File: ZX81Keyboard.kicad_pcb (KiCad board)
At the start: 2 copper layers, 153 x 58 mm, 52 parts, among them J2 Conn_01x05, J3 Conn_01x03, J4 Conn_01x08, SW1 1, SW10 0, SW11 Q, SW12 W, SW13 E, SW14 R, SW15 T, SW16 Y, SW17 U, SW18 I, SW19 O, SW2 2, SW20 P, SW21 A, SW22 S, SW23 D, SW24 F, SW25 G, SW26 H, SW27 J, SW28 K, SW29 L, SW3 3, SW30 NEW_LINE, SW31 SHIFT, SW32 Z, SW33 X, SW34 C, SW35 V, SW36 B, SW37 N, SW38 M, SW39 ., SW4 4, SW40 SPACE, SW5 5, SW6 6, SW7 7, SW8 8, SW9 9

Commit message: Nearing completion.
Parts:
- added G***: LOGO, zx81keyboard:title, F.Cu at (95.5, 69.8)
- moved G*** 37.7 mm to (71.4, 69.3)
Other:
- board text added: "+"
- board text added: "GND TURBO POWER"
- board text added: "J"
- board text added: "KA15 KA14 KA8 KA13 KA9 KA12 KA10 KA11"
- board text added: "KD0 KD1 KD2 KD3 KD4"
- board text removed: "ZX81 Tactile Keyboard"

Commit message: Nearing completion.
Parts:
- moved H1 0.71 mm to (65.5, 120.5)
- moved H2 0.71 mm to (212.0, 120.5)
- moved H3 0.71 mm to (65.5, 69.0)
- moved H4 0.71 mm to (212.0, 69.0)

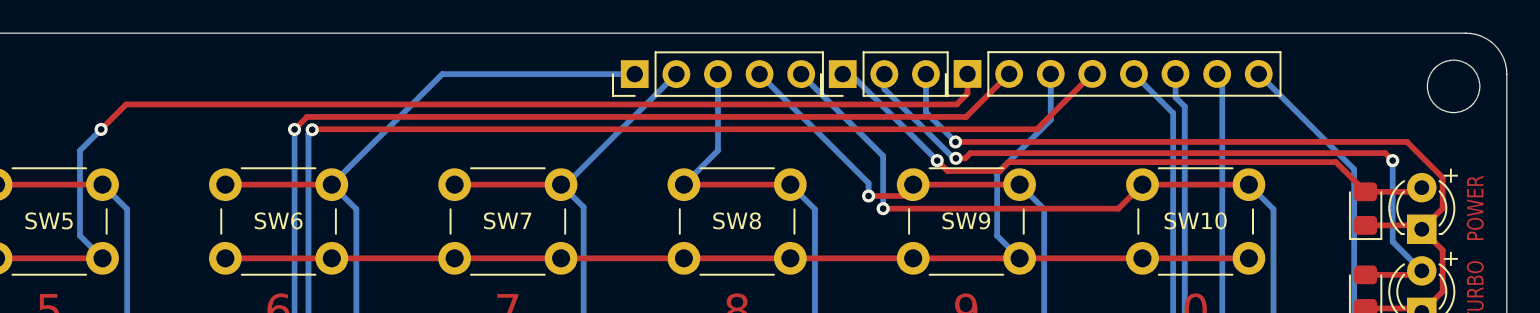
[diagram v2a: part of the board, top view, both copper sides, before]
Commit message: Fixed connector orientation.
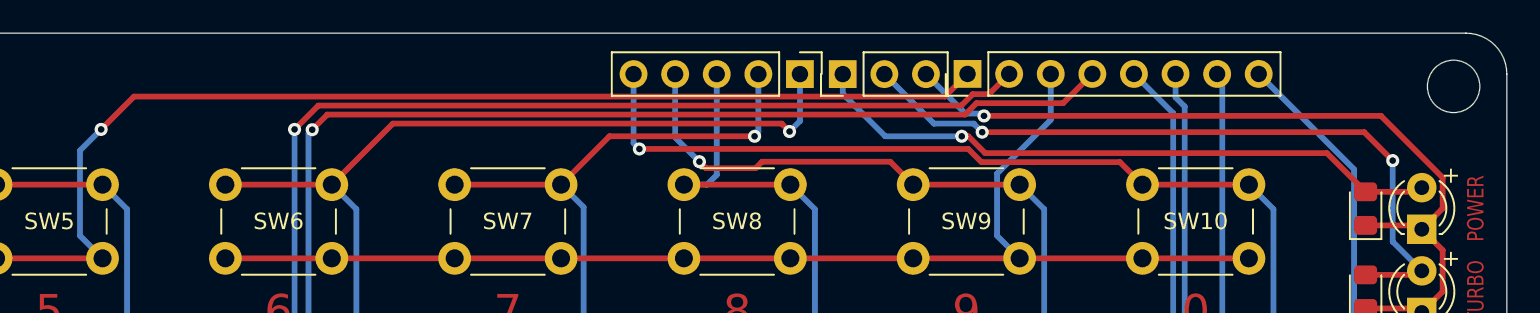
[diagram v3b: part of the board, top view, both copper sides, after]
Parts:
- moved J2 10.1 mm to (172.1, 68.2), turned to 270 degrees
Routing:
- net KD4: track 165.3 -> 177.5 mm, vias 0 -> 1
- net KD0: track 285.1 -> 294.7 mm
- net KD3: track 189.3 -> 196.4 mm, vias 0 -> 1
- net KD1: track 243.1 -> 249.8 mm
- net Net-(D1-Pad1): track 52.4 -> 51.0 mm
- net Net-(D2-Pad2): track 45.0 -> 44.2 mm
- net KD2: track 209.1 -> 209.9 mm
- net KA11: track 126.5 -> 125.8 mm
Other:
- board text added: "KD4 KD3 KD2 KD1 KD0"
- board text added: "ZX81 Tactile Keyboard Rev.2"
- board text removed: "KD0 KD1 KD2 KD3 KD4"
- board text removed: "ZX81 Tactile Keyboard Rev.1"
